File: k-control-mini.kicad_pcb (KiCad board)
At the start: 2 copper layers, 62.2 x 90 mm, 86 parts, among them J1_P1 IN_L, J1_P2 IN_GND, J1_P3 IN_R, J1_P4 OUT_R, J1_P5 OUT_GND, J1_P6 OUT_L, J2_P1 HP_R, J2_P2 HP_GND, J2_P3 HP_L, U1 H11L1S(TA)

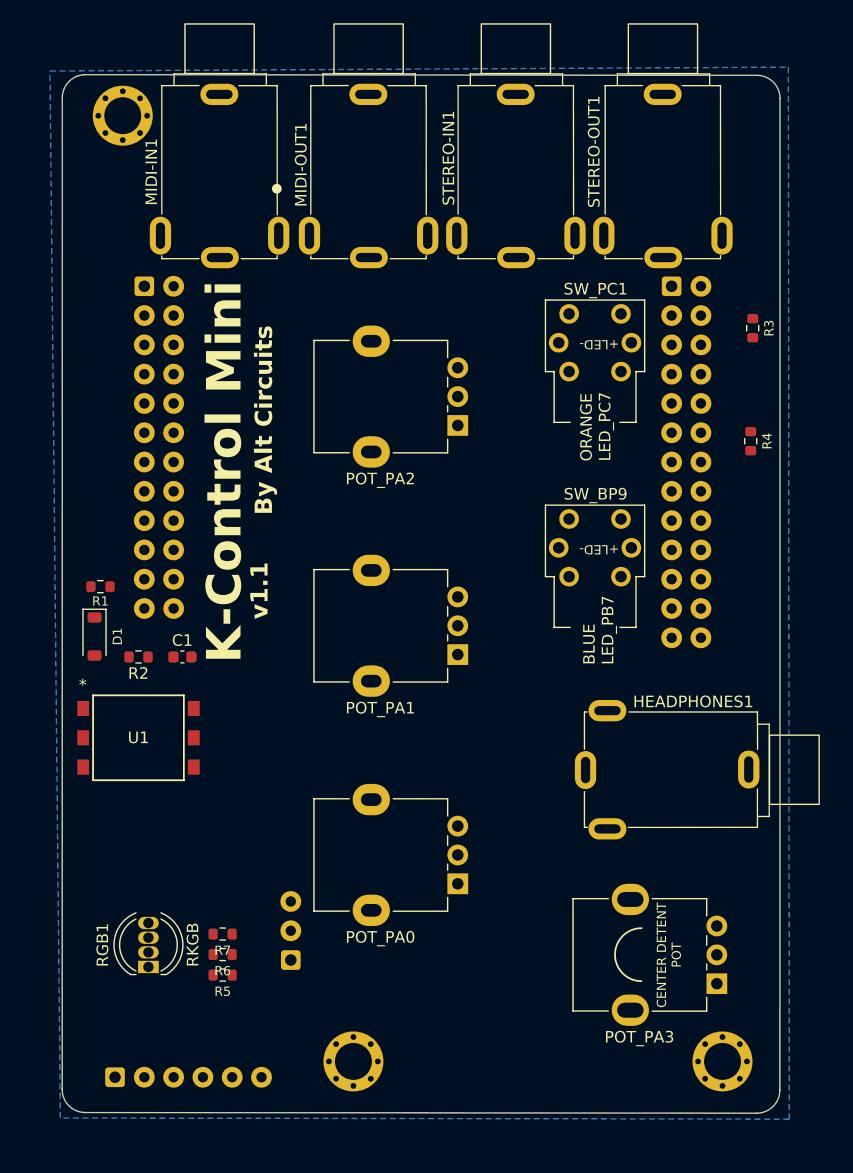
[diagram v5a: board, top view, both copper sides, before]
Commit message: fixed traces and silk screen
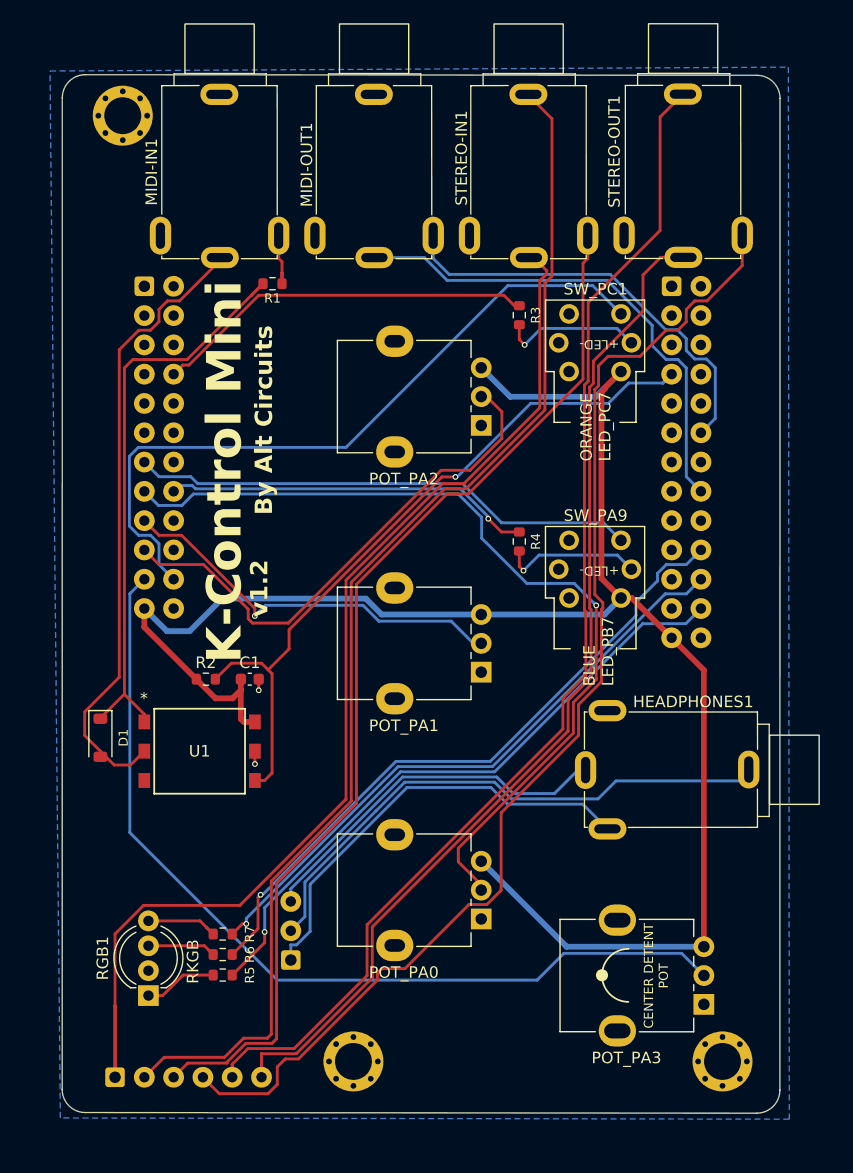
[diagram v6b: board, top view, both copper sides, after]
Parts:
- RGB1: footprint LED_THT:LED_D5.0mm-4_RGB -> LED_THT:LED_D5.0mm-4_RGB_Wide_Pins
- moved R1 30.2 mm to (135.6, 63.5)
- moved R4 21.9 mm to (157.0, 85.9)
- moved R3 20.3 mm to (157.0, 66.2)
- moved D1 8.80 mm to (120.7, 102.9)
- moved C1 6.15 mm to (133.6, 97.8)
- moved R2 6.15 mm to (129.8, 97.8), turned to 0 degrees
- moved U1 5.43 mm to (129.3, 104.0)
- moved POT_PA0 3.66 mm to (153.7, 118.6)
- moved POT_PA1 2.54 mm to (153.7, 97.2)
- moved RGB1 2.48 mm to (124.8, 125.2)
- moved POT_PA3 2.12 mm to (173.0, 126.0)
- moved POT_PA2 2.03 mm to (153.7, 75.8)
- moved SW_PA9 1.85 mm to (161.3, 90.8)
- moved STEREO-OUT1 1.75 mm to (172.4, 54.4)
- moved STEREO-IN1 1.10 mm to (159.0, 54.5)
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- renumbered SW_BP9 to SW_PA9
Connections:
- R5 pad 1: PA4 -> PA7
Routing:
- net +3.3V: track 0.00 -> 153.3 mm
- net IN_GND: track 0.00 -> 106.1 mm
- net OUT_R: track 0.00 -> 105.2 mm
- net OUT_GND: track 0.00 -> 105.0 mm
- net IN_L: track 0.00 -> 99.6 mm
- net IN_R: track 0.00 -> 93.2 mm
- net OUT_L: track 0.00 -> 91.3 mm
- net PA3: track 0.00 -> 79.3 mm
- net PA0: track 0.00 -> 75.6 mm, vias 0 -> 1
- net PC1: track 0.00 -> 64.4 mm
- net MIDI_RX: track 0.00 -> 63.9 mm, vias 0 -> 1
- net PA5: track 0.00 -> 58.7 mm, vias 0 -> 1
- net PA7: track 0.00 -> 56.5 mm, vias 0 -> 1
- net Net-(D1-A): track 0.00 -> 55.0 mm
- net PA6: track 0.00 -> 54.6 mm, vias 0 -> 1
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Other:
- board text added: "v${REVISION}"
- board text removed: "v1.1"

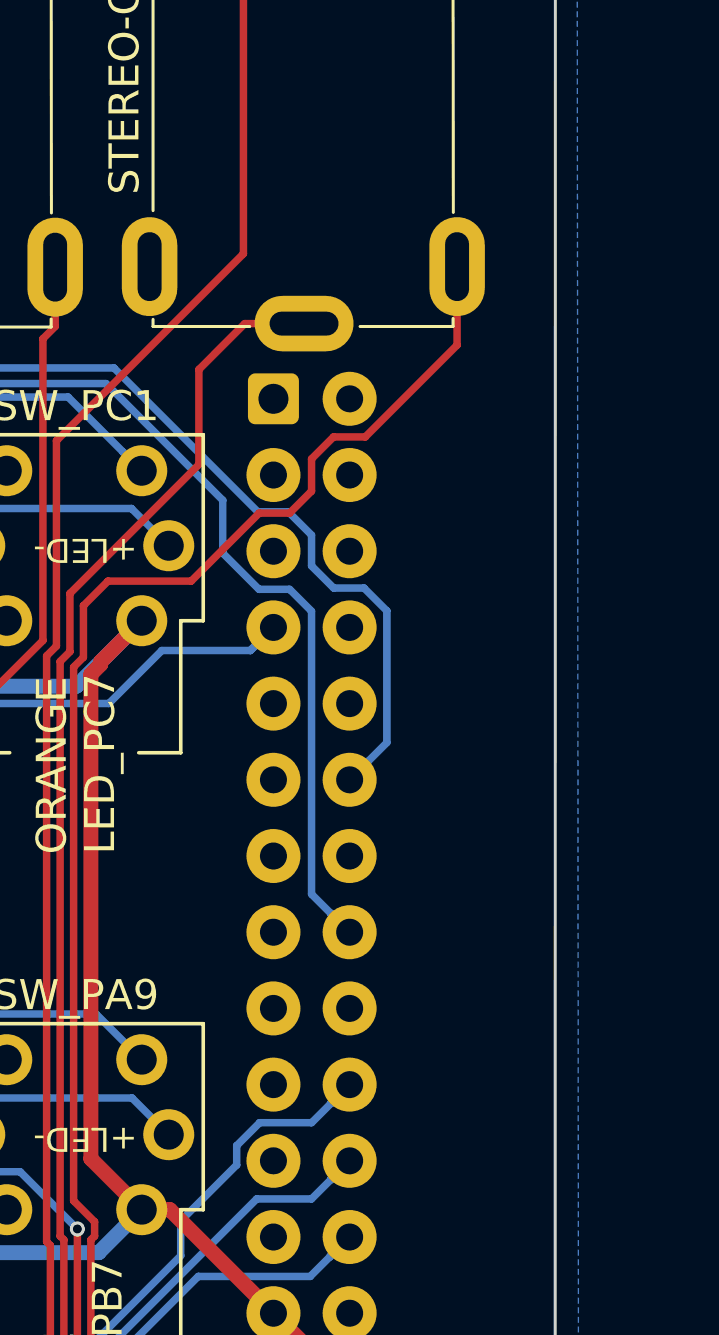
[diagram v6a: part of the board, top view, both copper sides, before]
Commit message: updated silkscreen and test patch
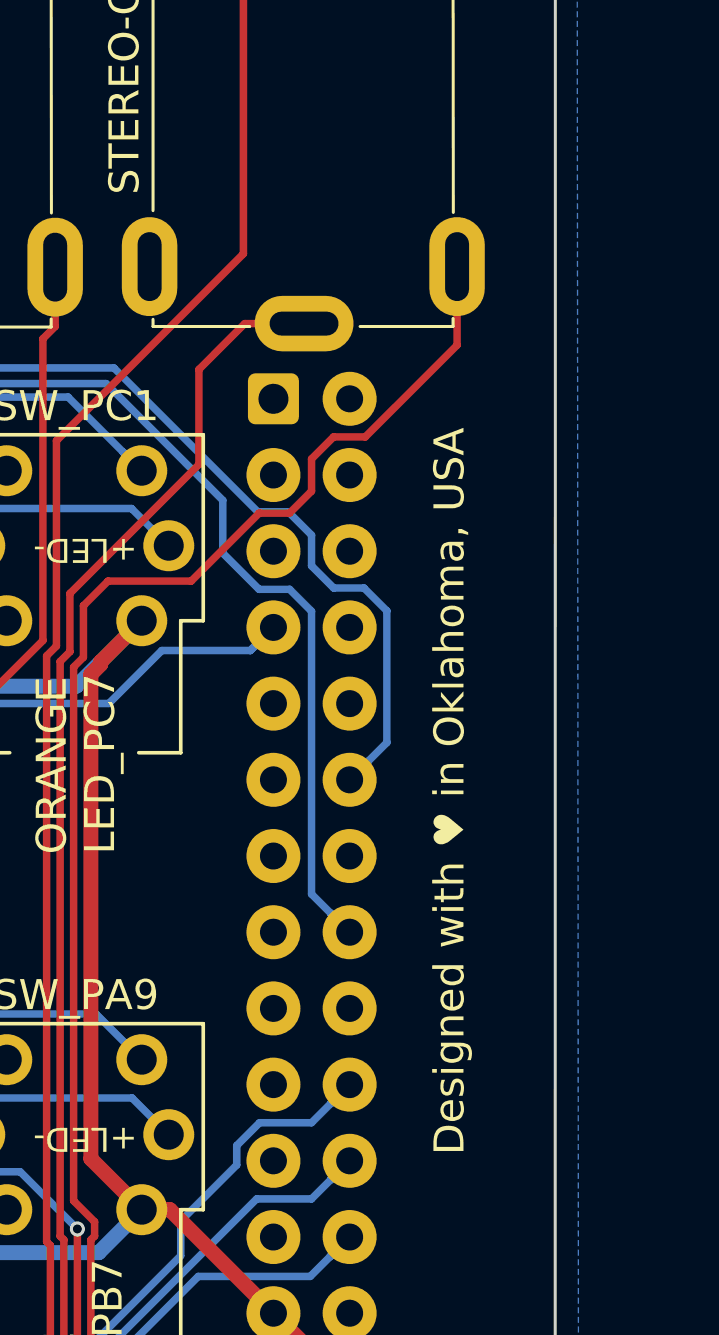
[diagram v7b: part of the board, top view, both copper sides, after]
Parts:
- moved G513513 14.8 mm to (155.1, 124.0)
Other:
- board text added: "Designed with ♥ in Oklahoma, USA"

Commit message: updates
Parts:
- moved HEADPHONES1 0.86 mm to (170.4, 106.9)
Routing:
- net PC1: track 64.4 -> 74.5 mm
- net GND: track 3.11 -> 12.3 mm, vias 2 -> 4
- net Net-(R4-Pad2): track 12.3 -> 19.9 mm
- net Net-(R3-Pad2): track 12.3 -> 16.4 mm
- net +3.3V: track 153.3 -> 156.8 mm
- net PA0: track 75.6 -> 78.9 mm
- net HP_L: track 36.0 -> 33.0 mm
- net PA1: track 34.8 -> 35.6 mm
- net HP_R: track 38.3 -> 39.2 mm
- net HP_GND: track 50.0 -> 49.3 mm
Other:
- board text added: "Designed with ♥ in Oklahoma"
- board text removed: "Designed with ♥ in Oklahoma, USA"
